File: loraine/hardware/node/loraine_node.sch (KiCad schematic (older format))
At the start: 45 parts, among them CON1 BARREL_JACK, IC1 ATTINY2313A-S, K1 LED1, K2 LED2, K3 LED3, P1 POWER_THRU, P2 POWER, P3 SOLDER_PAD, P4 BUS, P5 BUS_THRU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

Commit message: Prettified PCB
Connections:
- net LED0: now reaches IC1.12 ((PCINT0/AIN0)PB0), K3.2 (PM), R1.2
- net LED2: now reaches IC1.14 ((PCINT2/OC0A)PB2), K1.2 (PM), R3.2
- net A: now reaches P4.1 (P1), P5.1 (P1), U2.6 (A)
- net B: now reaches P4.2 (PM), P5.2 (PM), U2.7 (B)
- net CH4: now reaches P7.10, Q5.D
- net CH5: now reaches P7.12, Q6.D
- net CH6: now reaches P7.14, Q7.D
- net CH7: now reaches P7.16, Q8.D
- net CH0: now reaches P7.2, Q1.D
- net CH1: now reaches P7.4, Q2.D
- net CH2: now reaches P7.6, Q3.D
- net CH3: now reaches P7.8, Q4.D
- net MISO renamed LED6
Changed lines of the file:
@@
 	6050 4250 6050 2225
 Connection ~ 6050 4250
+Text Label 3025 7000 0    60   ~ 0
+B
+Text Label 3025 7150 0    60   ~ 0
+A
+Text Label 8650 1000 0    60   ~ 0
+CH0
+Text Label 8675 1600 0    60   ~ 0
+CH1
+Text Label 8675 2200 0    60   ~ 0
+CH2
+Text Label 8675 2800 0    60   ~ 0
+CH3
+Text Label 8700 3400 0    60   ~ 0
+CH4
+Text Label 8725 4000 0    60   ~ 0
+CH5
+Text Label 8550 4600 0    60   ~ 0
+CH6
+Text Label 8500 5200 0    60   ~ 0
+CH7
+Text Label 5225 1850 0    60   ~ 0
+LED0
+Text Label 5175 1475 0    60   ~ 0
+LED6
+Text Label 5125 1075 0    60   ~ 0
+LED2
 $EndSCHEMATC

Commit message: Adam's changes and gerbils
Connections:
- net GND: now also CON1.3
- no-connect marks 8 -> 7
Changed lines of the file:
@@
 NoConn ~ 4800 5050
 NoConn ~ 4800 5150
-NoConn ~ 1400 1250
 $Comp
 L PWR_FLAG #FLG025
@@
 Text Label 5125 1075 0    60   ~ 0
 LED2
+Wire Wire Line
+	1400 1250 1500 1250
+Wire Wire Line
+	1500 1250 1500 1350
+Connection ~ 1500 1350
 $EndSCHEMATC

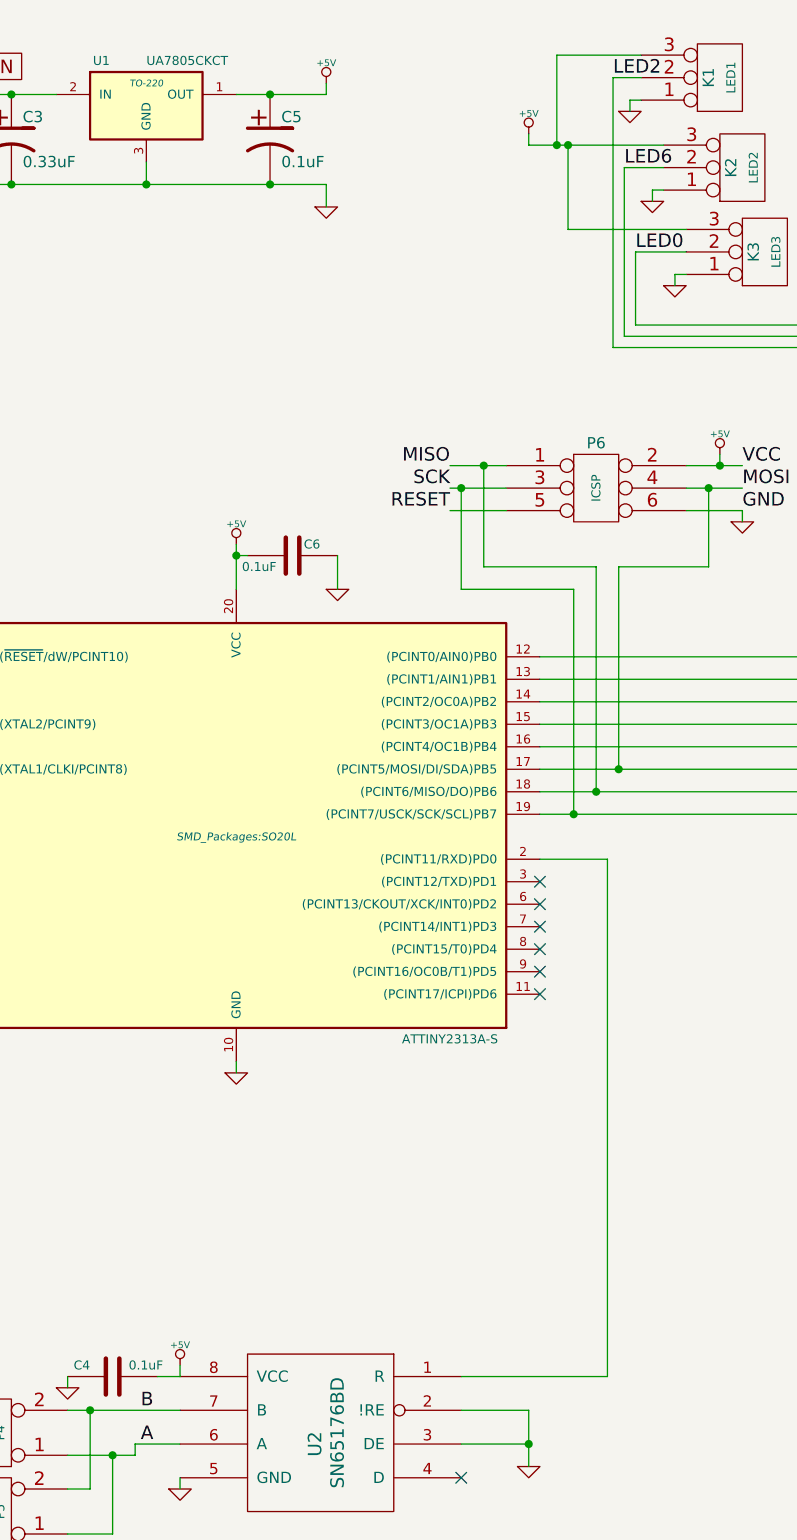
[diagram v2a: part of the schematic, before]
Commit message: Added TPs to node
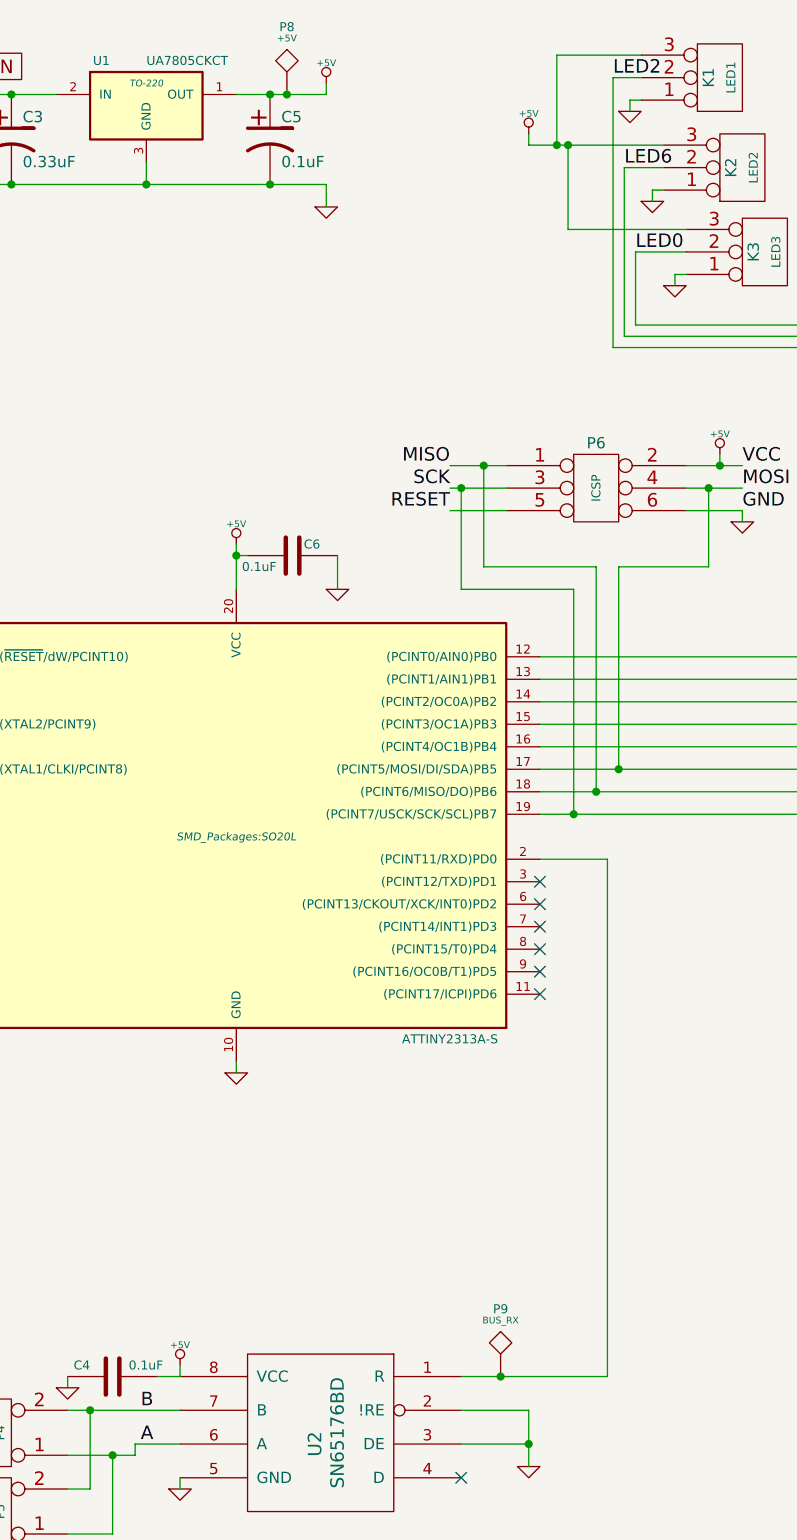
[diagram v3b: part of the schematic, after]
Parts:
- added P8: +5V, symbol TST
- added P9: BUS_RX, symbol TST
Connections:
- net +5V: now also P8.1
- net at IC1.2 ((PCINT11/RXD)PD0), U2.1 (R): now also P9.1
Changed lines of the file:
@@
 $EndComp
 $Comp
-L GND #PWR010
+L GND #PWR08
 U 1 1 5339D1EB
 P 2700 6900
-F 0 "#PWR010" H 2700 6900 30  0001 C CNN
+F 0 "#PWR08" H 2700 6900 30  0001 C CNN
 F 1 "GND" H 2700 6830 30  0001 C CNN
 F 2 "" H 2700 6900 60  0000 C CNN
@@
 $EndComp
 $Comp
-L GND #PWR014
+L GND #PWR09
 U 1 1 53790927
 P 5200 1225
-F 0 "#PWR014" H 5200 1225 30  0001 C CNN
+F 0 "#PWR09" H 5200 1225 30  0001 C CNN
 F 1 "GND" H 5200 1155 30  0001 C CNN
 F 2 "" H 5200 1225 60  0000 C CNN
@@
 $EndComp
 $Comp
-L GND #PWR015
+L GND #PWR010
 U 1 1 53790A46
 P 5300 1625
-F 0 "#PWR015" H 5300 1625 30  0001 C CNN
+F 0 "#PWR010" H 5300 1625 30  0001 C CNN
 F 1 "GND" H 5300 1555 30  0001 C CNN
 F 2 "" H 5300 1625 60  0000 C CNN
@@
 $EndComp
 $Comp
-L GND #PWR016
+L GND #PWR011
 U 1 1 53790B67
 P 5400 2000
-F 0 "#PWR016" H 5400 2000 30  0001 C CNN
+F 0 "#PWR011" H 5400 2000 30  0001 C CNN
 F 1 "GND" H 5400 1930 30  0001 C CNN
 F 2 "" H 5400 2000 60  0000 C CNN
@@
 $EndComp
 $Comp
-L GND #PWR017
+L GND #PWR012
 U 1 1 53C70517
 P 7800 1450
-F 0 "#PWR017" H 7800 1450 30  0001 C CNN
+F 0 "#PWR012" H 7800 1450 30  0001 C CNN
 F 1 "GND" H 7800 1380 30  0001 C CNN
 F 2 "" H 7800 1450 60  0000 C CNN
@@
 $EndComp
 $Comp
-L GND #PWR018
+L GND #PWR013
 U 1 1 53CC8831
 P 7800 2050
-F 0 "#PWR018" H 7800 2050 30  0001 C CNN
+F 0 "#PWR013" H 7800 2050 30  0001 C CNN
 F 1 "GND" H 7800 1980 30  0001 C CNN
 F 2 "" H 7800 2050 60  0000 C CNN
@@
 $EndComp
 $Comp
-L GND #PWR019
+L GND #PWR014
 U 1 1 53CC8B29
 P 7800 2650
-F 0 "#PWR019" H 7800 2650 30  0001 C CNN
+F 0 "#PWR014" H 7800 2650 30  0001 C CNN
 F 1 "GND" H 7800 2580 30  0001 C CNN
 F 2 "" H 7800 2650 60  0000 C CNN
@@
 $EndComp
 $Comp
-L GND #PWR020
+L GND #PWR015
 U 1 1 53CC8D3E
 P 7800 3250
-F 0 "#PWR020" H 7800 3250 30  0001 C CNN
+F 0 "#PWR015" H 7800 3250 30  0001 C CNN
 F 1 "GND" H 7800 3180 30  0001 C CNN
 F 2 "" H 7800 3250 60  0000 C CNN
@@
 $EndComp
 $Comp
-L GND #PWR021
+L GND #PWR016
 U 1 1 53CC8F35
 P 7800 3850
-F 0 "#PWR021" H 7800 3850 30  0001 C CNN
+F 0 "#PWR016" H 7800 3850 30  0001 C CNN
 F 1 "GND" H 7800 3780 30  0001 C CNN
 F 2 "" H 7800 3850 60  0000 C CNN
@@
 $EndComp
 $Comp
-L GND #PWR022
+L GND #PWR017
 U 1 1 53CC937A
 P 7800 4450
-F 0 "#PWR022" H 7800 4450 30  0001 C CNN
+F 0 "#PWR017" H 7800 4450 30  0001 C CNN
 F 1 "GND" H 7800 4380 30  0001 C CNN
 F 2 "" H 7800 4450 60  0000 C CNN
@@
 $EndComp
 $Comp
-L GND #PWR023
+L GND #PWR018
 U 1 1 53CC988A
 P 7800 5050
-F 0 "#PWR023" H 7800 5050 30  0001 C CNN
+F 0 "#PWR018" H 7800 5050 30  0001 C CNN
 F 1 "GND" H 7800 4980 30  0001 C CNN
 F 2 "" H 7800 5050 60  0000 C CNN
@@
 $EndComp
 $Comp
-L GND #PWR024
+L GND #PWR019
 U 1 1 53CC9B10
 P 7800 5650
-F 0 "#PWR024" H 7800 5650 30  0001 C CNN
+F 0 "#PWR019" H 7800 5650 30  0001 C CNN
 F 1 "GND" H 7800 5580 30  0001 C CNN
 F 2 "" H 7800 5650 60  0000 C CNN
@@
 NoConn ~ 4800 5150
 $Comp
-L PWR_FLAG #FLG025
+L PWR_FLAG #FLG020
 U 1 1 53CCE243
 P 1750 1150
-F 0 "#FLG025" H 1750 1245 30  0001 C CNN
+F 0 "#FLG020" H 1750 1245 30  0001 C CNN
 F 1 "PWR_FLAG" H 1750 1330 30  0000 C CNN
 F 2 "" H 1750 1150 60  0000 C CNN
@@
 Connection ~ 1750 1150
 $Comp
-L +5V #PWR026
+L +5V #PWR021
 U 1 1 53CD0C96
 P 3850 1100
-F 0 "#PWR026" H 3850 1190 20  0001 C CNN
+F 0 "#PWR021" H 3850 1190 20  0001 C CNN
 F 1 "+5V" H 3850 1190 30  0000 C CNN
 F 2 "" H 3850 1100 60  0000 C CNN
@@
 $EndComp
 $Comp
-L +5V #PWR027
+L +5V #PWR022
 U 1 1 53CD0F28
 P 3450 3150
-F 0 "#PWR027" H 3450 3240 20  0001 C CNN
+F 0 "#PWR022" H 3450 3240 20  0001 C CNN
 F 1 "+5V" H 3450 3240 30  0000 C CNN
 F 2 "" H 3450 3150 60  0000 C CNN
@@
 $EndComp
 $Comp
-L +5V #PWR028
+L +5V #PWR023
 U 1 1 53CD1362
 P 3200 6800
-F 0 "#PWR028" H 3200 6890 20  0001 C CNN
+F 0 "#PWR023" H 3200 6890 20  0001 C CNN
 F 1 "+5V" H 3200 6890 30  0000 C CNN
 F 2 "" H 3200 6800 60  0000 C CNN
@@
 $EndComp
 $Comp
-L +5V #PWR029
+L +5V #PWR024
 U 1 1 53CD1481
 P 5600 2750
-F 0 "#PWR029" H 5600 2840 20  0001 C CNN
+F 0 "#PWR024" H 5600 2840 20  0001 C CNN
 F 1 "+5V" H 5600 2840 30  0000 C CNN
 F 2 "" H 5600 2750 60  0000 C CNN
@@
 	10275 5150 10375 5150
 $Comp
-L +5V #PWR?
+L +5V #PWR025
 U 1 1 53CD6C0A
 P 4750 1325
-F 0 "#PWR?" H 4750 1415 20  0001 C CNN
+F 0 "#PWR025" H 4750 1415 20  0001 C CNN
 F 1 "+5V" H 4750 1415 30  0000 C CNN
 F 2 "" H 4750 1325 60  0000 C CNN
@@
 	1500 1250 1500 1350
 Connection ~ 1500 1350
+$Comp
+L TST P8
+U 1 1 53D64AE3
+P 3675 1150
+F 0 "P8" H 3675 1450 40  0000 C CNN
+F 1 "+5V" H 3675 1400 30  0000 C CNN
+F 2 "" H 3675 1150 60  0000 C CNN
+F 3 "" H 3675 1150 60  0000 C CNN
+	1    3675 1150
+	1    0    0    -1
+$EndComp
+Connection ~ 3675 1150
+$Comp
+L TST P9
+U 1 1 53D6514B
+P 4625 6850
+F 0 "P9" H 4625 7150 40  0000 C CNN
+F 1 "BUS_RX" H 4625 7100 30  0000 C CNN
+F 2 "" H 4625 6850 60  0000 C CNN
+F 3 "" H 4625 6850 60  0000 C CNN
+	1    4625 6850
+	1    0    0    -1
+$EndComp
+Connection ~ 4625 6850
 $EndSCHEMATC
